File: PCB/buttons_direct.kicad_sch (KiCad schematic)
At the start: 9 parts

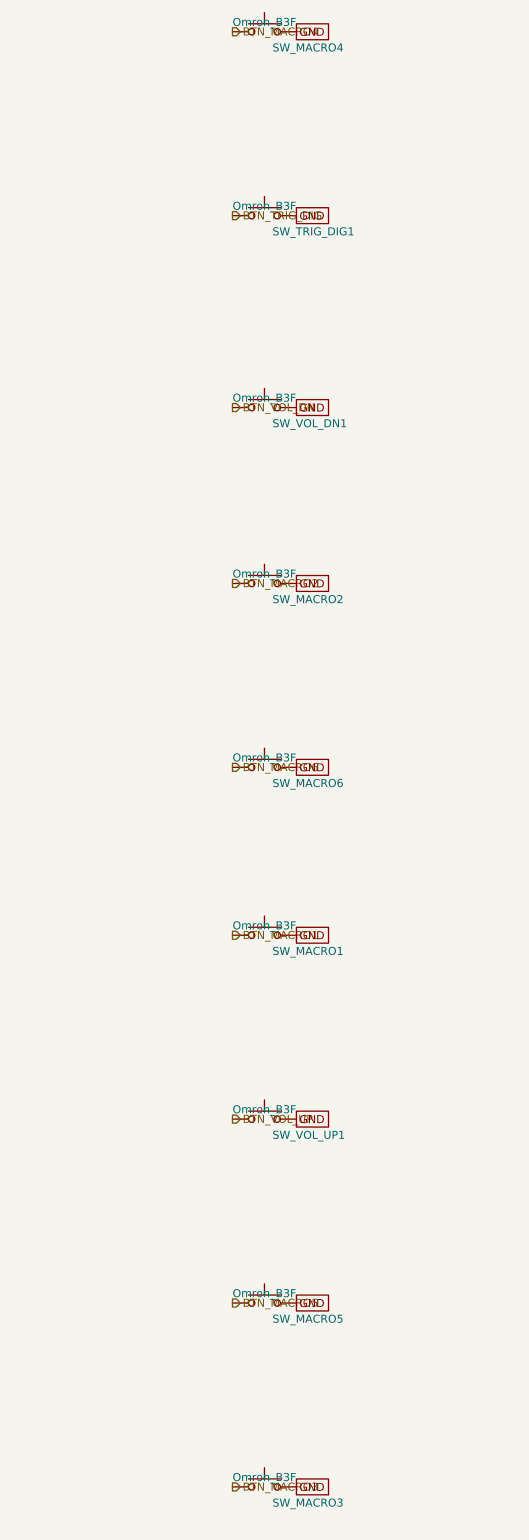
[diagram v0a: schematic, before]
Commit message: refactor: updated gulikit footprint
This updates the gulikit thumbstick footprint to be accurate.
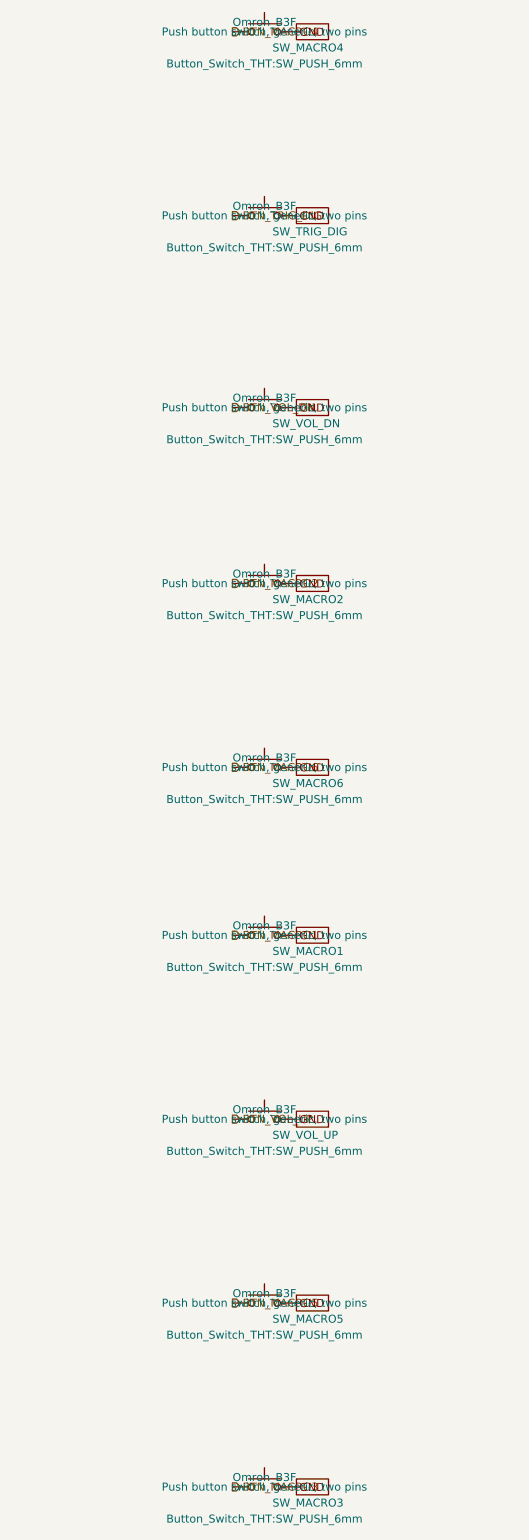
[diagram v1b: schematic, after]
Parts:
- removed SW_TRIG_DIG1, SW_VOL_DN1, SW_VOL_UP1: Omron_B3F, Button_Switch_THT:SW_PUSH_6mm, symbol Switch:SW_Push
- added SW_TRIG_DIG, SW_VOL_DN, SW_VOL_UP: Omron_B3F, Button_Switch_THT:SW_PUSH_6mm, symbol Switch:SW_Push
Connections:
- net BTN_TRIG_DIG: now also SW_TRIG_DIG.1
- net BTN_VOL_DN: now also SW_VOL_DN.1
- net BTN_VOL_UP: now also SW_VOL_UP.1
- net GND: now also SW_TRIG_DIG.2, SW_VOL_DN.2, SW_VOL_UP.2

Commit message: layout: beginning pcb layout
This updates the schematic with a few different footprints while also starts the layout.
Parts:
- SW_MACRO1, SW_MACRO2, SW_MACRO3, SW_MACRO4, SW_MACRO5, SW_MACRO6: footprint Button_Switch_THT:SW_PUSH_6mm -> Button_Switch_SMD:SW_Push_1TS009xxxx-xxxx-xxxx_6x6x5mm
- SW_TRIG_DIG1: renamed from SW_TRIG_DIG; footprint Button_Switch_THT:SW_PUSH_6mm -> Button_Switch_SMD:SW_Push_1P1T-MP_NO_Horizontal_Alps_SKRTLAE010
- SW_VOL_DN1: renamed from SW_VOL_DN; footprint Button_Switch_THT:SW_PUSH_6mm -> Button_Switch_SMD:SW_Push_1P1T-MP_NO_Horizontal_Alps_SKRTLAE010
- SW_VOL_UP1: renamed from SW_VOL_UP; footprint Button_Switch_THT:SW_PUSH_6mm -> Button_Switch_SMD:SW_Push_1P1T-MP_NO_Horizontal_Alps_SKRTLAE010
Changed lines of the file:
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@@
 			)
 		)
-		(property "Footprint" "Button_Switch_THT:SW_PUSH_6mm"
+		(property "Footprint" "Button_Switch_SMD:SW_Push_1TS009xxxx-xxxx-xxxx_6x6x5mm"
 			(at 148.59 226.06 0)
 			(show_name no)
@@
 		)
 		(instances
-			(project ""
-				(path "/d0f5b7d7-b2b6-4492-958c-e60265d3c6b4/e5523a34-26e6-4606-a95c-f5d6b5b43fdf"
+			(project "snips_controller"
+				(path "/868f8289-8434-4465-b2f4-2accc5e40bab/e5523a34-26e6-4606-a95c-f5d6b5b43fdf"
 					(reference "SW_MACRO3")
 					(unit 1)
 				)
 			)
+			(project ""
+				(path "/d0f5b7d7-b2b6-4492-958c-e60265d3c6b4/e5523a34-26e6-4606-a95c-f5d6b5b43fdf"
+					(reference "SW_MACRO3")
+					(unit 1)
+				)
+			)
 		)
 	)
@@
 		(dnp no)
 		(fields_autoplaced yes)
-		(property "Reference" "SW_VOL_UP"
+		(property "Reference" "SW_VOL_UP1"
 			(at 149.86 165.1 0)
 			(show_name no)
@@
 			)
 		)
-		(property "Footprint" "Button_Switch_THT:SW_PUSH_6mm"
+		(property "Footprint" "Button_Switch_SMD:SW_Push_1P1T-MP_NO_Horizontal_Alps_SKRTLAE010"
 			(at 148.59 167.64 0)
 			(show_name no)
@@
 		)
 		(instances
+			(project "snips_controller"
+				(path "/868f8289-8434-4465-b2f4-2accc5e40bab/e5523a34-26e6-4606-a95c-f5d6b5b43fdf"
+					(reference "SW_VOL_UP1")
+					(unit 1)
+				)
+			)
 			(project ""
 				(path "/d0f5b7d7-b2b6-4492-958c-e60265d3c6b4/e5523a34-26e6-4606-a95c-f5d6b5b43fdf"
@@
 			)
 		)
-		(property "Footprint" "Button_Switch_THT:SW_PUSH_6mm"
+		(property "Footprint" "Button_Switch_SMD:SW_Push_1TS009xxxx-xxxx-xxxx_6x6x5mm"
 			(at 148.59 111.76 0)
 			(show_name no)
@@
 		)
 		(instances
-			(project ""
-				(path "/d0f5b7d7-b2b6-4492-958c-e60265d3c6b4/e5523a34-26e6-4606-a95c-f5d6b5b43fdf"
+			(project "snips_controller"
+				(path "/868f8289-8434-4465-b2f4-2accc5e40bab/e5523a34-26e6-4606-a95c-f5d6b5b43fdf"
 					(reference "SW_MACRO6")
 					(unit 1)
 				)
 			)
+			(project ""
+				(path "/d0f5b7d7-b2b6-4492-958c-e60265d3c6b4/e5523a34-26e6-4606-a95c-f5d6b5b43fdf"
+					(reference "SW_MACRO6")
+					(unit 1)
+				)
+			)
 		)
 	)
@@
 		(dnp no)
 		(fields_autoplaced yes)
-		(property "Reference" "SW_VOL_DN"
+		(property "Reference" "SW_VOL_DN1"
 			(at 149.86 52.07 0)
 			(show_name no)
@@
 			)
 		)
-		(property "Footprint" "Button_Switch_THT:SW_PUSH_6mm"
+		(property "Footprint" "Button_Switch_SMD:SW_Push_1P1T-MP_NO_Horizontal_Alps_SKRTLAE010"
 			(at 148.59 54.61 0)
 			(show_name no)
@@
 		)
 		(instances
+			(project "snips_controller"
+				(path "/868f8289-8434-4465-b2f4-2accc5e40bab/e5523a34-26e6-4606-a95c-f5d6b5b43fdf"
+					(reference "SW_VOL_DN1")
+					(unit 1)
+				)
+			)
 			(project ""
 				(path "/d0f5b7d7-b2b6-4492-958c-e60265d3c6b4/e5523a34-26e6-4606-a95c-f5d6b5b43fdf"
@@
 			)
 		)
-		(property "Footprint" "Button_Switch_THT:SW_PUSH_6mm"
+		(property "Footprint" "Button_Switch_SMD:SW_Push_1TS009xxxx-xxxx-xxxx_6x6x5mm"
 			(at 148.59 -5.08 0)
 			(show_name no)
@@
 		)
 		(instances
-			(project ""
-				(path "/d0f5b7d7-b2b6-4492-958c-e60265d3c6b4/e5523a34-26e6-4606-a95c-f5d6b5b43fdf"
+			(project "snips_controller"
+				(path "/868f8289-8434-4465-b2f4-2accc5e40bab/e5523a34-26e6-4606-a95c-f5d6b5b43fdf"
 					(reference "SW_MACRO4")
 					(unit 1)
 				)
 			)
+			(project ""
+				(path "/d0f5b7d7-b2b6-4492-958c-e60265d3c6b4/e5523a34-26e6-4606-a95c-f5d6b5b43fdf"
+					(reference "SW_MACRO4")
+					(unit 1)
+				)
+			)
 		)
 	)
@@
 		(dnp no)
 		(fields_autoplaced yes)
-		(property "Reference" "SW_TRIG_DIG"
+		(property "Reference" "SW_TRIG_DIG1"
 			(at 149.86 21.59 0)
 			(show_name no)
@@
 			)
 		)
-		(property "Footprint" "Button_Switch_THT:SW_PUSH_6mm"
+		(property "Footprint" "Button_Switch_SMD:SW_Push_1P1T-MP_NO_Horizontal_Alps_SKRTLAE010"
 			(at 148.59 24.13 0)
 			(show_name no)
@@
 		)
 		(instances
+			(project "snips_controller"
+				(path "/868f8289-8434-4465-b2f4-2accc5e40bab/e5523a34-26e6-4606-a95c-f5d6b5b43fdf"
+					(reference "SW_TRIG_DIG1")
+					(unit 1)
+				)
+			)
 			(project ""
 				(path "/d0f5b7d7-b2b6-4492-958c-e60265d3c6b4/e5523a34-26e6-4606-a95c-f5d6b5b43fdf"
@@
 			)
 		)
-		(property "Footprint" "Button_Switch_THT:SW_PUSH_6mm"
+		(property "Footprint" "Button_Switch_SMD:SW_Push_1TS009xxxx-xxxx-xxxx_6x6x5mm"
 			(at 148.59 82.55 0)
 			(show_name no)
@@
 		)
 		(instances
+			(project "snips_controller"
+				(path "/868f8289-8434-4465-b2f4-2accc5e40bab/e5523a34-26e6-4606-a95c-f5d6b5b43fdf"
+					(reference "SW_MACRO2")
+					(unit 1)
+				)
+			)
 			(project ""
 				(path "/d0f5b7d7-b2b6-4492-958c-e60265d3c6b4/e5523a34-26e6-4606-a95c-f5d6b5b43fdf"
@@
 			)
 		)
-		(property "Footprint" "Button_Switch_THT:SW_PUSH_6mm"
+		(property "Footprint" "Button_Switch_SMD:SW_Push_1TS009xxxx-xxxx-xxxx_6x6x5mm"
 			(at 148.59 138.43 0)
 			(show_name no)
@@
 		)
 		(instances
+			(project "snips_controller"
+				(path "/868f8289-8434-4465-b2f4-2accc5e40bab/e5523a34-26e6-4606-a95c-f5d6b5b43fdf"
+					(reference "SW_MACRO1")
+					(unit 1)
+				)
+			)
 			(project ""
 				(path "/d0f5b7d7-b2b6-4492-958c-e60265d3c6b4/e5523a34-26e6-4606-a95c-f5d6b5b43fdf"
@@
 			)
 		)
-		(property "Footprint" "Button_Switch_THT:SW_PUSH_6mm"
+		(property "Footprint" "Button_Switch_SMD:SW_Push_1TS009xxxx-xxxx-xxxx_6x6x5mm"
 			(at 148.59 196.85 0)
 			(show_name no)
@@
 		)
 		(instances
-			(project ""
-				(path "/d0f5b7d7-b2b6-4492-958c-e60265d3c6b4/e5523a34-26e6-4606-a95c-f5d6b5b43fdf"
+			(project "snips_controller"
+				(path "/868f8289-8434-4465-b2f4-2accc5e40bab/e5523a34-26e6-4606-a95c-f5d6b5b43fdf"
+					(reference "SW_MACRO5")
+					(unit 1)
+				)
+			)
+			(project ""
+				(path "/d0f5b7d7-b2b6-4492-958c-e60265d3c6b4/e5523a34-26e6-4606-a95c-f5d6b5b43fdf"
